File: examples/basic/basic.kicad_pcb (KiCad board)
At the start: 2 copper layers, 9 x 14 mm, 7 parts

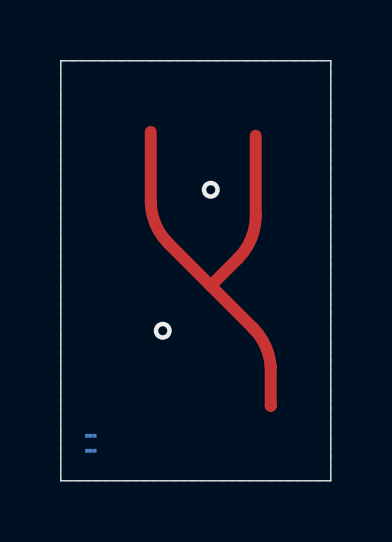
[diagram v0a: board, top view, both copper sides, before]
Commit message: Huge rewrite to enhance functionality and fix some limitations
- Allow for selection of input and output folders.
- Added settings for:
    - Adjusting xy offset of port positions.
    - Settings to control nanomesh quality when converting gerbers to images.
    - Unified 0 indexing for simulation ports in KiCAD schematic and python scripts.
    - Allow adjusting smoothing ratio for mesh lines.
    - Stackup layers moved from separate "fab/stackup.json" to inside "simulation.json".
    - Backup gerber files and simulation.json config inside simulation output to keep track of parametric search changes in schematic.
    - Output visualisation of gerber to image mesh for debugging semi-buggy nanomesh workflow where there will be unwanted merging of nets.
    - Added option for dielectric layers to use a gerber file as mesh.
    - Added option to repeat layer for given z-heights.
- Fixed examples/* to reflect modifications to gerber2ems.
- Added examples/differential_hatched as additional example.
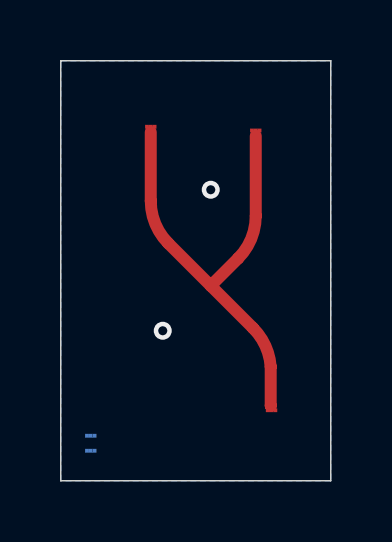
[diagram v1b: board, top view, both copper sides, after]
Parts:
- added SP2: Simulation_Port, antmicro-footprints:NetTie-2_SMD_Pad0.127mm, F.Cu at (146.5, 103.3)
- SP0: renamed from TP1; value Net-Tie_2 -> Simulation_Port
- SP1: renamed from TP3; value Net-Tie_2 -> Simulation_Port
- moved SP0 0.30 mm to (143.0, 103.2), turned to 180 degrees
- moved SP1 0.25 mm to (147.0, 112.7), turned to 0 degrees

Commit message: Update examples with corrected settings and keep track of exported gerbers
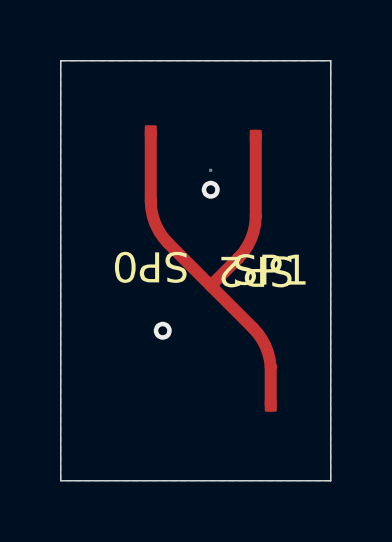
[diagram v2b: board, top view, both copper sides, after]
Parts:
- removed the SP1 at (147.0, 112.7)
- removed the SP1 at (143.0, 103.2)
- removed the SP2 at (146.5, 103.3)
- removed the SP2 at (147.0, 112.8)
- removed SP3: Simulation_Port, antmicro-footprints:Simulation_Port
- removed TP2, TP4: Net-Tie_2, antmicro-footprints:NetTie-2_SMD_Pad0.127mm
- added SP1: Simulation_Port, simulation_port:pad_0.4mm, F.Cu at (147.0, 112.5)
- added SP2: Simulation_Port, simulation_port:pad_0.4mm, F.Cu at (146.5, 103.5)
- added TP1: TestPoint, simulation_port:pad_0.1mm, B.Cu at (145.0, 104.7)
- SP0: footprint antmicro-footprints:NetTie-2_SMD_Pad0.127mm -> simulation_port:pad_0.4mm
- moved SP0 0.15 mm to (143.0, 103.3)
